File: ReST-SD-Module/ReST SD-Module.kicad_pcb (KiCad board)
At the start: 2 copper layers, 18.7 x 28.7 mm, 6 parts, among them CON1 uSD_Card, P1 CONN_02X05

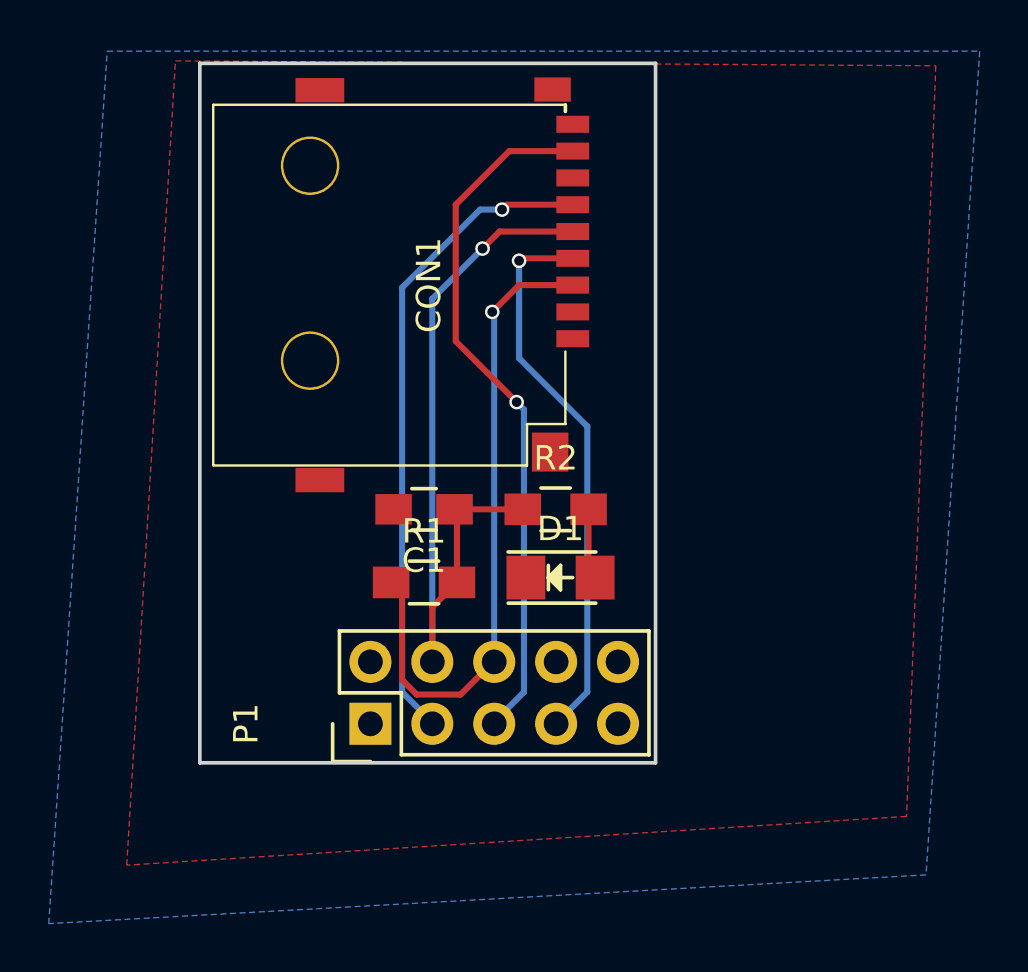
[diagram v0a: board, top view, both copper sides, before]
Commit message: Finally removed all unnecessary Libs and added Heatsink for 5V Regulator
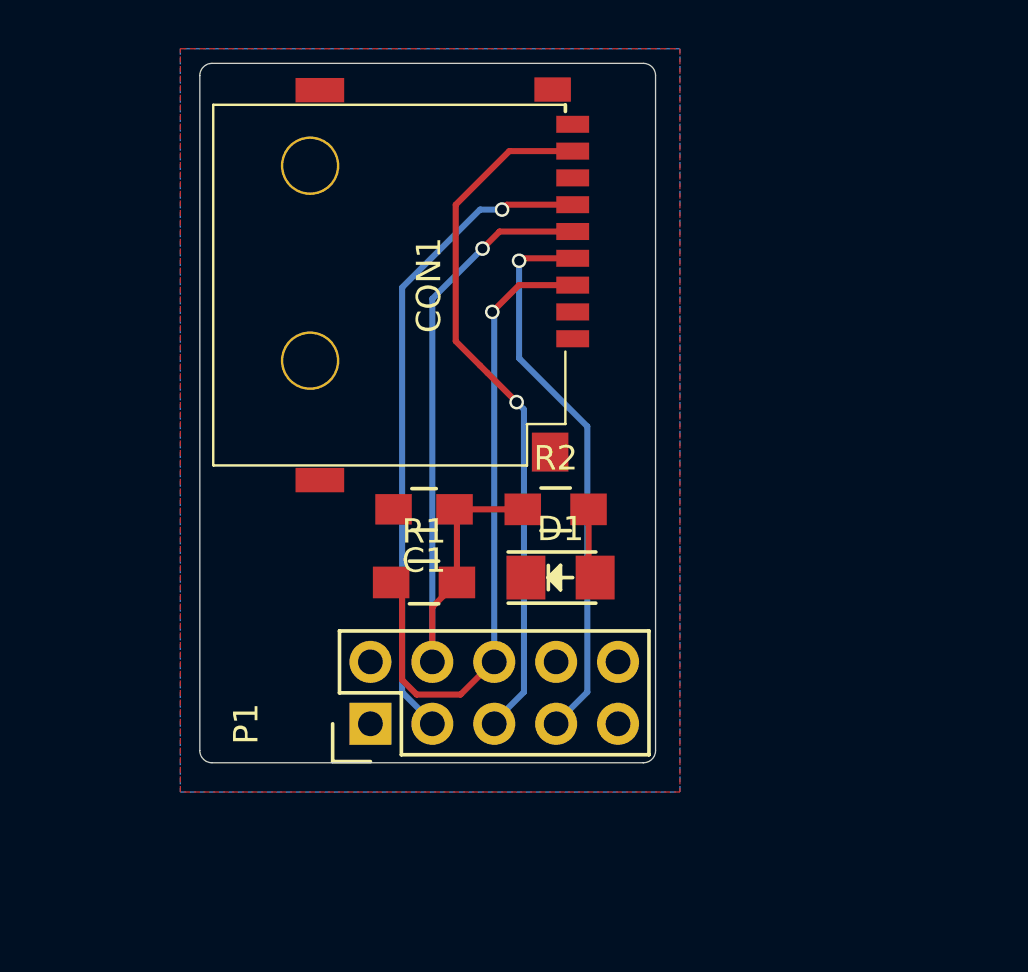
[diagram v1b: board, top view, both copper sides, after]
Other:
- outline, holes or cut-outs redrawn
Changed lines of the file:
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@@
     (links 17)
     (no_connects 0)
-    (area 134.724999 81.024999 153.575001 109.875001)
+    (area 134.794999 81.094999 153.505001 109.805001)
     (thickness 1.6)
-    (drawings 4)
+    (drawings 8)
     (tracks 51)
     (zones 0)
@@
     (trace_min 0.2)
     (segment_width 0.2)
-    (edge_width 0.15)
+    (edge_width 0.01)
     (via_size 0.6)
     (via_drill 0.4)
@@
     (pad_to_mask_clearance 0.2)
     (aux_axis_origin 0 0)
-    (visible_elements FFFFFF7F)
+    (visible_elements 7FFFFFFF)
     (pcbplotparams
       (layerselection 0x00030_80000001)
@@
     )
   )
-  (gr_line (start 134.8 109.8) (end 153.5 109.8) (angle 90) (layer Edge.Cuts) (width 0.15))
-  (gr_line (start 134.8 81.1) (end 134.8 109.8) (angle 90) (layer Edge.Cuts) (width 0.15))
-  (gr_line (start 153.5 81.1) (end 134.8 81.1) (angle 90) (layer Edge.Cuts) (width 0.15))
-  (gr_line (start 153.5 109.8) (end 153.5 81.1) (angle 90) (layer Edge.Cuts) (width 0.15))
+  (gr_arc (start 135.3 109.3) (end 135.3 109.8) (angle 90) (layer Edge.Cuts) (width 0.01))
+  (gr_arc (start 153 109.3) (end 153.5 109.3) (angle 90) (layer Edge.Cuts) (width 0.01))
+  (gr_arc (start 153 81.6) (end 153 81.1) (angle 90) (layer Edge.Cuts) (width 0.01))
+  (gr_arc (start 135.3 81.6) (end 134.8 81.6) (angle 90) (layer Edge.Cuts) (width 0.01))
+  (gr_line (start 134.8 109.3) (end 134.8 81.6) (angle 90) (layer Edge.Cuts) (width 0.01))
+  (gr_line (start 153 109.8) (end 135.3 109.8) (angle 90) (layer Edge.Cuts) (width 0.01))
+  (gr_line (start 153.5 81.6) (end 153.5 109.3) (angle 90) (layer Edge.Cuts) (width 0.01))
+  (gr_line (start 135.3 81.1) (end 153 81.1) (angle 90) (layer Edge.Cuts) (width 0.01))
   (segment (start 144.34 105.66) (end 144.34 90.76) (width 0.25) (layer B.Cu) (net 1))
   (segment (start 147.1 88) (end 150.1 88) (width 0.25) (layer F.Cu) (net 1))
@@
     (polygon
       (pts
-        (xy 133.8 81) (xy 165 81.2) (xy 163.8 112) (xy 131.8 114)
+        (xy 154.5 111) (xy 134 111) (xy 134 80.5) (xy 154.5 80.5)
       )
     )
@@
     (polygon
       (pts
-        (xy 131 80.6) (xy 166.8 80.6) (xy 164.6 114.4) (xy 128.6 116.4)
+        (xy 154.5 80.5) (xy 134 80.5) (xy 134 111) (xy 154.5 111)
       )
     )

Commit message: Added IRLML2502 Module and added Ground vias everywhere
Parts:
- added 11: VIA-0.6mm, ReST-Library:VIA-0.6mm, F.Cu at (137.0, 100.5)
- added 111: VIA-0.6mm, ReST-Library:VIA-0.6mm, F.Cu at (152.2, 93.8)
- added 1111: VIA-0.6mm, ReST-Library:VIA-0.6mm, F.Cu at (137.5, 88.0)
- added 1112: VIA-0.6mm, ReST-Library:VIA-0.6mm, F.Cu at (137.5, 90.0)
- added 1121: VIA-0.6mm, ReST-Library:VIA-0.6mm, F.Cu at (139.5, 88.0)
- added 1122: VIA-0.6mm, ReST-Library:VIA-0.6mm, F.Cu at (139.5, 90.0)
- added 113: VIA-0.6mm, ReST-Library:VIA-0.6mm, F.Cu at (152.2, 95.8)
- added 1131: VIA-0.6mm, ReST-Library:VIA-0.6mm, F.Cu at (141.5, 88.0)
- added 1132: VIA-0.6mm, ReST-Library:VIA-0.6mm, F.Cu at (141.5, 90.0)
- added 15: VIA-0.6mm, ReST-Library:VIA-0.6mm, F.Cu at (137.0, 104.5)
- added 23: VIA-0.6mm, ReST-Library:VIA-0.6mm, F.Cu at (138.0, 102.5)
- added 31: VIA-0.6mm, ReST-Library:VIA-0.6mm, F.Cu at (139.0, 100.5)
- added 35: VIA-0.6mm, ReST-Library:VIA-0.6mm, F.Cu at (139.0, 104.5)
- added 43: VIA-0.6mm, ReST-Library:VIA-0.6mm, F.Cu at (140.0, 102.5)
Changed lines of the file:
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@@
 (kicad_pcb (version 4) (host pcbnew 4.0.1-stable)
   (general
-    (links 17)
+    (links 31)
     (no_connects 0)
     (area 134.794999 81.094999 153.505001 109.805001)
@@
     (tracks 51)
     (zones 0)
-    (modules 6)
+    (modules 20)
     (nets 8)
   )
@@
     (mod_text_size 1 1)
     (mod_text_width 0.15)
-    (pad_size 1.524 1.524)
-    (pad_drill 0.762)
+    (pad_size 0.6 0.6)
+    (pad_drill 0.4)
     (pad_to_mask_clearance 0.2)
     (aux_axis_origin 0 0)
@@
     (add_net "Net-(D1-Pad2)")
   )
+  (module ReST-Library:VIA-0.6mm (layer F.Cu)
+    (at 152.25 95.75)
+    (fp_text reference 113 (at 0 3.5) (layer F.SilkS) hide
+      (effects (font (size 1 1) (thickness 0.15)))
+    )
+    (fp_text value VIA-0.6mm (at 0 -3) (layer F.Fab) hide
+      (effects (font (size 1 1) (thickness 0.15)))
+    )
+    (pad 1 thru_hole circle (at 0 0) (size 0.6 0.6) (drill 0.4) (layers *.Cu)
+      (net 2 GND) (zone_connect 2))
+  )
+  (module ReST-Library:VIA-0.6mm (layer F.Cu)
+    (at 152.25 93.75)
+    (fp_text reference 111 (at 0 3.5) (layer F.SilkS) hide
+      (effects (font (size 1 1) (thickness 0.15)))
+    )
+    (fp_text value VIA-0.6mm (at 0 -3) (layer F.Fab) hide
+      (effects (font (size 1 1) (thickness 0.15)))
+    )
+    (pad 1 thru_hole circle (at 0 0) (size 0.6 0.6) (drill 0.4) (layers *.Cu)
+      (net 2 GND) (zone_connect 2))
+  )
+  (module ReST-Library:VIA-0.6mm (layer F.Cu)
+    (at 141.5 90)
+    (fp_text reference 1132 (at 0 3.5) (layer F.SilkS) hide
+      (effects (font (size 1 1) (thickness 0.15)))
+    )
+    (fp_text value VIA-0.6mm (at 0 -3) (layer F.Fab) hide
+      (effects (font (size 1 1) (thickness 0.15)))
+    )
+    (pad 1 thru_hole circle (at 0 0) (size 0.6 0.6) (drill 0.4) (layers *.Cu)
+      (net 2 GND) (zone_connect 2))
+  )
+  (module ReST-Library:VIA-0.6mm (layer F.Cu)
+    (at 139.5 90)
+    (fp_text reference 1122 (at 0 3.5) (layer F.SilkS) hide
+      (effects (font (size 1 1) (thickness 0.15)))
+    )
+    (fp_text value VIA-0.6mm (at 0 -3) (layer F.Fab) hide
+      (effects (font (size 1 1) (thickness 0.15)))
+    )
+    (pad 1 thru_hole circle (at 0 0) (size 0.6 0.6) (drill 0.4) (layers *.Cu)
+      (net 2 GND) (zone_connect 2))
+  )
+  (module ReST-Library:VIA-0.6mm (layer F.Cu)
+    (at 137.5 90)
+    (fp_text reference 1112 (at 0 3.5) (layer F.SilkS) hide
+      (effects (font (size 1 1) (thickness 0.15)))
+    )
+    (fp_text value VIA-0.6mm (at 0 -3) (layer F.Fab) hide
+      (effects (font (size 1 1) (thickness 0.15)))
+    )
+    (pad 1 thru_hole circle (at 0 0) (size 0.6 0.6) (drill 0.4) (layers *.Cu)
+      (net 2 GND) (zone_connect 2))
+  )
+  (module ReST-Library:VIA-0.6mm (layer F.Cu)
+    (at 141.5 88)
+    (fp_text reference 1131 (at 0 3.5) (layer F.SilkS) hide
+      (effects (font (size 1 1) (thickness 0.15)))
+    )
+    (fp_text value VIA-0.6mm (at 0 -3) (layer F.Fab) hide
+      (effects (font (size 1 1) (thickness 0.15)))
+    )
+    (pad 1 thru_hole circle (at 0 0) (size 0.6 0.6) (drill 0.4) (layers *.Cu)
+      (net 2 GND) (zone_connect 2))
+  )
+  (module ReST-Library:VIA-0.6mm (layer F.Cu)
+    (at 139.5 88)
+    (fp_text reference 1121 (at 0 3.5) (layer F.SilkS) hide
+      (effects (font (size 1 1) (thickness 0.15)))
+    )
+    (fp_text value VIA-0.6mm (at 0 -3) (layer F.Fab) hide
+      (effects (font (size 1 1) (thickness 0.15)))
+    )
+    (pad 1 thru_hole circle (at 0 0) (size 0.6 0.6) (drill 0.4) (layers *.Cu)
+      (net 2 GND) (zone_connect 2))
+  )
+  (module ReST-Library:VIA-0.6mm (layer F.Cu)
+    (at 137.5 88)
+    (fp_text reference 1111 (at 0 3.5) (layer F.SilkS) hide
+      (effects (font (size 1 1) (thickness 0.15)))
+    )
+    (fp_text value VIA-0.6mm (at 0 -3) (layer F.Fab) hide
+      (effects (font (size 1 1) (thickness 0.15)))
+    )
+    (pad 1 thru_hole circle (at 0 0) (size 0.6 0.6) (drill 0.4) (layers *.Cu)
+      (net 2 GND) (zone_connect 2))
+  )
+  (module ReST-Library:VIA-0.6mm (layer F.Cu)
+    (at 139 104.5)
+    (fp_text reference 35 (at 0 3.5) (layer F.SilkS) hide
+      (effects (font (size 1 1) (thickness 0.15)))
+    )
+    (fp_text value VIA-0.6mm (at 0 -3) (layer F.Fab) hide
+      (effects (font (size 1 1) (thickness 0.15)))
+    )
+    (pad 1 thru_hole circle (at 0 0) (size 0.6 0.6) (drill 0.4) (layers *.Cu)
+      (net 2 GND) (zone_connect 2))
+  )
+  (module ReST-Library:VIA-0.6mm (layer F.Cu)
+    (at 137 104.5)
+    (fp_text reference 15 (at 0 3.5) (layer F.SilkS) hide
+      (effects (font (size 1 1) (thickness 0.15)))
+    )
+    (fp_text value VIA-0.6mm (at 0 -3) (layer F.Fab) hide
+      (effects (font (size 1 1) (thickness 0.15)))
+    )
+    (pad 1 thru_hole circle (at 0 0) (size 0.6 0.6) (drill 0.4) (layers *.Cu)
+      (net 2 GND) (zone_connect 2))
+  )
+  (module ReST-Library:VIA-0.6mm (layer F.Cu)
+    (at 140 102.5)
+    (fp_text reference 43 (at 0 3.5) (layer F.SilkS) hide
+      (effects (font (size 1 1) (thickness 0.15)))
+    )
+    (fp_text value VIA-0.6mm (at 0 -3) (layer F.Fab) hide
+      (effects (font (size 1 1) (thickness 0.15)))
+    )
+    (pad 1 thru_hole circle (at 0 0) (size 0.6 0.6) (drill 0.4) (layers *.Cu)
+      (net 2 GND) (zone_connect 2))
+  )
+  (module ReST-Library:VIA-0.6mm (layer F.Cu)
+    (at 138 102.5)
+    (fp_text reference 23 (at 0 3.5) (layer F.SilkS) hide
+      (effects (font (size 1 1) (thickness 0.15)))
+    )
+    (fp_text value VIA-0.6mm (at 0 -3) (layer F.Fab) hide
+      (effects (font (size 1 1) (thickness 0.15)))
+    )
+    (pad 1 thru_hole circle (at 0 0) (size 0.6 0.6) (drill 0.4) (layers *.Cu)
+      (net 2 GND) (zone_connect 2))
+  )
+  (module ReST-Library:VIA-0.6mm (layer F.Cu)
+    (at 139 100.5)
+    (fp_text reference 31 (at 0 3.5) (layer F.SilkS) hide
+      (effects (font (size 1 1) (thickness 0.15)))
+    )
+    (fp_text value VIA-0.6mm (at 0 -3) (layer F.Fab) hide
+      (effects (font (size 1 1) (thickness 0.15)))
+    )
+    (pad 1 thru_hole circle (at 0 0) (size 0.6 0.6) (drill 0.4) (layers *.Cu)
+      (net 2 GND) (zone_connect 2))
+  )
   (module Capacitors_SMD:C_0805_HandSoldering (layer F.Cu)
     (at 144 99.4 180)
@@
     )
   )
+  (module ReST-Library:VIA-0.6mm (layer F.Cu)
+    (at 137 100.5)
+    (fp_text reference 11 (at 0 3.5) (layer F.SilkS) hide
+      (effects (font (size 1 1) (thickness 0.15)))
+    )
+    (fp_text value VIA-0.6mm (at 0 -3) (layer F.Fab) hide
+      (effects (font (size 1 1) (thickness 0.15)))
+    )
+    (pad 1 thru_hole circle (at 0 0) (size 0.6 0.6) (drill 0.4) (layers *.Cu)
+      (net 2 GND) (zone_connect 2))
+  )
   (gr_arc (start 135.3 109.3) (end 135.3 109.8) (angle 90) (layer Edge.Cuts) (width 0.01))

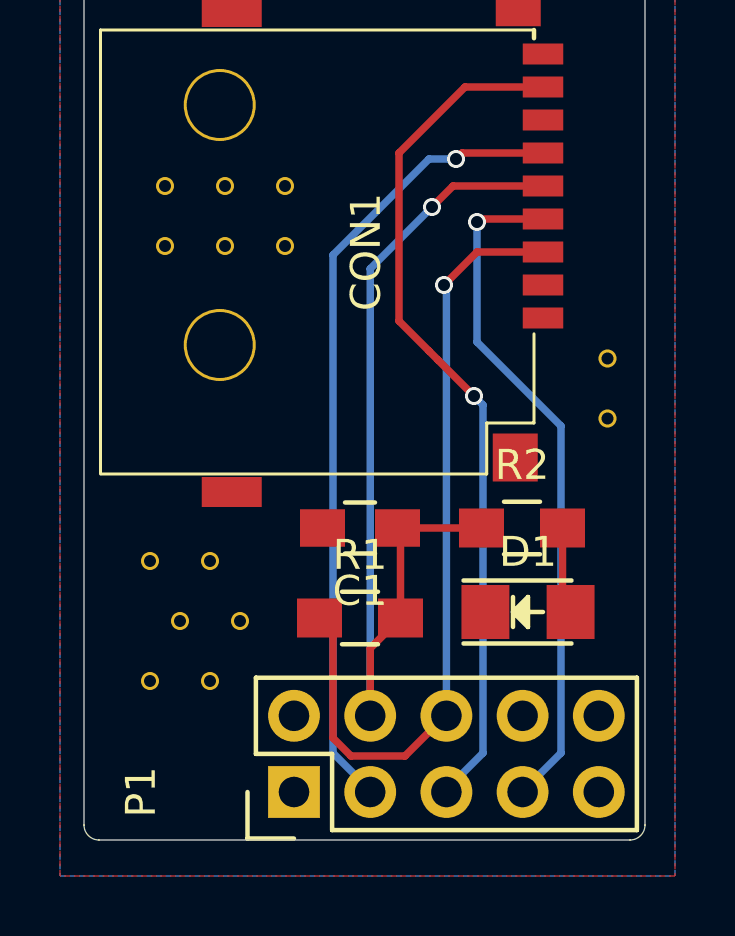
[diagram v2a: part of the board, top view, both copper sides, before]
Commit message: Finished PCB design, notations and silkscreen
gonna work to finish a combined design for cheaper pcb cost and put
everything i need into the bom
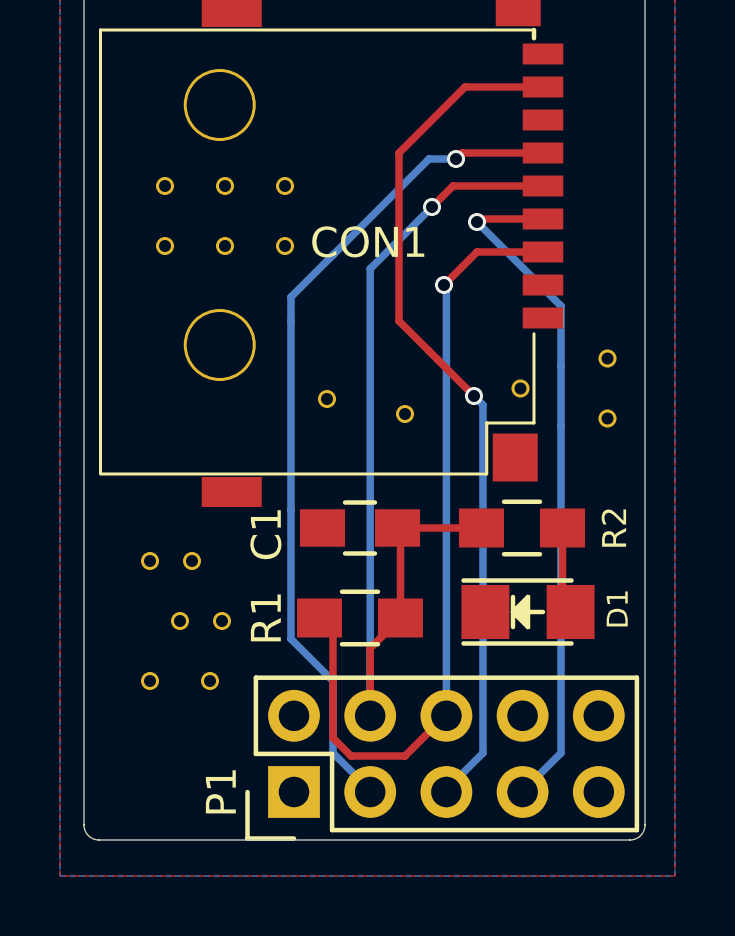
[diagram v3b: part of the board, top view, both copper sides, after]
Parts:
- added ?: , ReST-Library:VIA-0.6mm, F.Cu at (149.3, 94.8)
- added ?: , ReST-Library:Logo_silk_OSHW_6x6mm, B.Cu at (145.1, 84.8)
- added ?: , ReST-Library:STM32-6mm, B.Cu at (145.4, 98.9)
- added ?: , ReST-Library:VIA-0.6mm, F.Cu at (142.9, 95.1)
- added ?: , ReST-Library:VIA-0.6mm, F.Cu at (145.5, 95.6)
- ?: renamed from 1121; value VIA-0.6mm -> (none)
- ?: renamed from 1111; value VIA-0.6mm -> (none)
- ?: renamed from 35; value VIA-0.6mm -> (none)
- ?: renamed from 15; value VIA-0.6mm -> (none)
- ?: renamed from 43; value VIA-0.6mm -> (none)
- ?: renamed from 23; value VIA-0.6mm -> (none)
- ?: renamed from 31; value VIA-0.6mm -> (none)
- ?: renamed from 11; value VIA-0.6mm -> (none)
- ?: renamed from 113; value VIA-0.6mm -> (none)
- ?: renamed from 111; value VIA-0.6mm -> (none)
- ?: renamed from 1132; value VIA-0.6mm -> (none)
- ?: renamed from 1122; value VIA-0.6mm -> (none)
- ?: renamed from 1112; value VIA-0.6mm -> (none)
- ?: renamed from 1131; value VIA-0.6mm -> (none)
- C1: value 100nF -> (none)
- CON1: value uSD_Card -> (none)
- D1: value Led_Small -> (none)
- P1: value CONN_02X05 -> (none)
- R1: value 10K -> (none)
- R2: value 150R -> (none)
- moved ? 0.60 mm to (139.4, 102.5)
- moved ? 0.60 mm to (138.4, 100.5)
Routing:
- net /SPI-SCK: track 27.1 -> 28.2 mm
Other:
- board text added: "ReST SD Card Adapter Rev. A @maker_berry"

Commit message: Final release
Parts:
- moved P1 0.11 mm to (141.8, 108.1)
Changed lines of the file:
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@@
     (links 34)
     (no_connects 0)
-    (area 134.794999 81.094999 153.505001 109.805001)
+    (area 134 80.5 154.500001 111.000001)
     (thickness 1.6)
     (drawings 9)
-    (tracks 57)
+    (tracks 59)
     (zones 0)
     (modules 25)
@@
     (visible_elements 7FFFFFFF)
     (pcbplotparams
-      (layerselection 0x00030_80000001)
-      (usegerberextensions false)
+      (layerselection 0x010f0_80000001)
+      (usegerberextensions true)
       (excludeedgelayer true)
       (linewidth 0.100000)
@@
       (psa4output false)
       (plotreference true)
-      (plotvalue true)
+      (plotvalue false)
       (plotinvisibletext false)
       (padsonsilk false)
@@
       (outputformat 1)
       (mirror false)
-      (drillshape 1)
+      (drillshape 0)
       (scaleselection 1)
-      (outputdirectory ""))
+      (outputdirectory "../Gerber/SD Adapter/"))
   )
   (net 0 "")
@@
   )
   (module Pin_Headers:Pin_Header_Straight_2x05 (layer F.Cu)
-    (at 141.8 108.2 90)
+    (at 141.85 108.1 90)
     (descr "Through hole pin header")
     (tags "pin header")
@@
   (segment (start 144.34 105.66) (end 144.34 103.41) (width 0.25) (layer F.Cu) (net 1))
   (segment (start 144.34 103.41) (end 145.35 102.4) (width 0.25) (layer F.Cu) (net 1))
+  (segment (start 146.93 105.56) (end 145.69 106.8) (width 0.25) (layer F.Cu) (net 3))
+  (segment (start 145.69 106.8) (end 143.5 106.8) (width 0.25) (layer F.Cu) (net 3))
+  (segment (start 143.5 106.8) (end 143.1 106.4) (width 0.25) (layer F.Cu) (net 3))
   (segment (start 146.88 105.66) (end 146.88 91.38) (width 0.25) (layer B.Cu) (net 3))
   (segment (start 147.9 90.2) (end 150.1 90.2) (width 0.25) (layer F.Cu) (net 3))
@@
   (segment (start 146.88 91.38) (end 146.8 91.3) (width 0.25) (layer B.Cu) (net 3))
   (segment (start 146.88 105.66) (end 146.84 105.66) (width 0.25) (layer F.Cu) (net 3))
-  (segment (start 146.84 105.66) (end 145.5 107) (width 0.25) (layer F.Cu) (net 3))
-  (segment (start 145.5 107) (end 143.7 107) (width 0.25) (layer F.Cu) (net 3))
-  (segment (start 143.7 107) (end 143.1 106.4) (width 0.25) (layer F.Cu) (net 3))
   (segment (start 143.1 106.4) (end 143.1 102.85) (width 0.25) (layer F.Cu) (net 3))
   (segment (start 143.1 102.85) (end 142.65 102.4) (width 0.25) (layer F.Cu) (net 3))
@@
   (segment (start 143.1 90.3) (end 146.3 87.1) (width 0.25) (layer B.Cu) (net 5))
   (segment (start 144.34 108.2) (end 144.34 107.96) (width 0.25) (layer B.Cu) (net 5))
+  (segment (start 148.1 95.3) (end 148.15 95.35) (width 0.25) (layer B.Cu) (net 6))
+  (segment (start 148.15 95.35) (end 148.15 106.85) (width 0.25) (layer B.Cu) (net 6))
+  (segment (start 148.15 106.85) (end 148.1 106.9) (width 0.25) (layer B.Cu) (net 6))
   (segment (start 146.88 108.2) (end 146.88 108.12) (width 0.25) (layer B.Cu) (net 6))
   (segment (start 146.88 108.12) (end 148.1 106.9) (width 0.25) (layer B.Cu) (net 6))
-  (segment (start 148.1 106.9) (end 148.1 95.3) (width 0.25) (layer B.Cu) (net 6))
   (segment (start 148.1 95.3) (end 147.8 95) (width 0.25) (layer B.Cu) (net 6))
   (via (at 147.8 95) (size 0.6) (drill 0.4) (layers F.Cu B.Cu) (net 6))
